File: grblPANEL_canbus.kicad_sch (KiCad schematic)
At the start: 14 parts, among them J301 Conn_01x02, U301 SN65HVD230

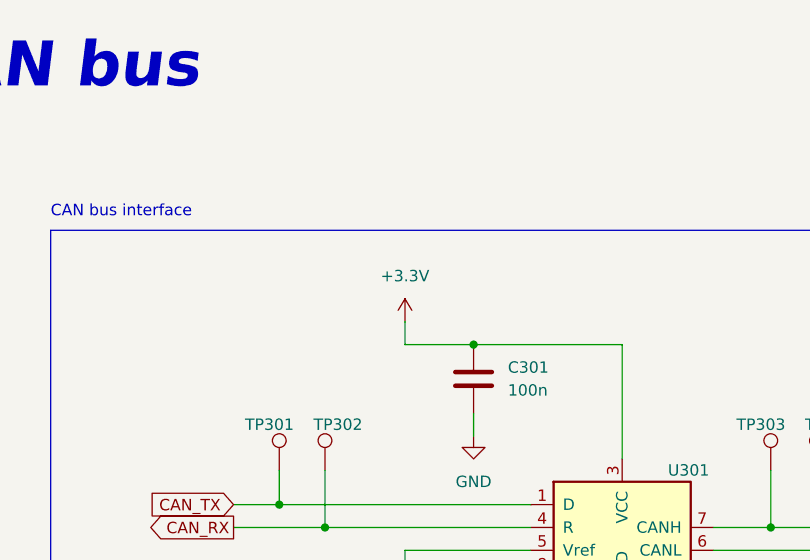
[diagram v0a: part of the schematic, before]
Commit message: ERC fixes
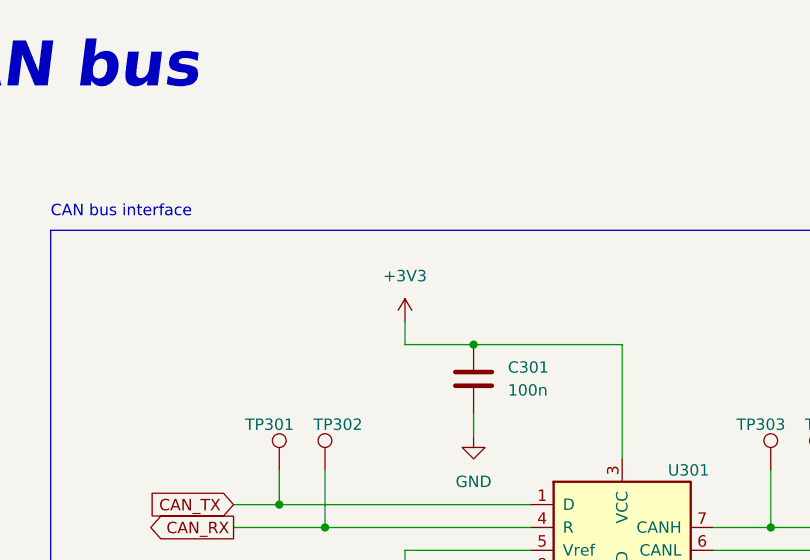
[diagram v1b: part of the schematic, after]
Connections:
- net +3.3V renamed +3V3
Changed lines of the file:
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@@
-    (pin "1")
-  )
-  (symbol (lib_id "power:+3.3V") (at 85.09 50.8 0) (unit 1)
-    (in_bom yes) (on_board yes) (fields_autoplaced)
-    (property "Reference" "#PWR0301" (id 0) (at 85.09 54.61 0)
-      (effects (font (size 1.27 1.27)) hide)
-    )
-    (property "Value" "+3.3V" (id 1) (at 85.09 45.72 0))
-    (property "Footprint" "" (id 2) (at 85.09 50.8 0)
-      (effects (font (size 1.27 1.27)) hide)
-    )
-    (property "Datasheet" "" (id 3) (at 85.09 50.8 0)
-      (effects (font (size 1.27 1.27)) hide)
-    )
     (pin "1")
   )
@@
     (pin "2")
   )
+  (symbol (lib_id "power:+3V3") (at 85.09 50.8 0) (unit 1)
+    (in_bom yes) (on_board yes) (fields_autoplaced)
+    (property "Reference" "#PWR0107" (id 0) (at 85.09 54.61 0)
+      (effects (font (size 1.27 1.27)) hide)
+    )
+    (property "Value" "+3V3" (id 1) (at 85.09 45.72 0))
+    (property "Footprint" "" (id 2) (at 85.09 50.8 0)
+      (effects (font (size 1.27 1.27)) hide)
+    )
+    (property "Datasheet" "" (id 3) (at 85.09 50.8 0)
+      (effects (font (size 1.27 1.27)) hide)
+    )
+    (pin "1")
+  )
 )

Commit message: Refresh
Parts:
- C301, C302, C303: footprint (none) -> Capacitor_SMD:C_0603_1608Metric
- D301: footprint (none) -> Package_TO_SOT_SMD:SOT-23
- J301: footprint (none) -> TerminalBlock_4Ucon:TerminalBlock_4Ucon_1x02_P3.50mm_Horizontal
- JP301: footprint (none) -> Connector_Pin:Pin_D1.1mm_L8.5mm_W2.5mm_FlatFork
- R301, R302, R303: footprint (none) -> Resistor_SMD:R_0603_1608Metric
- TP301, TP302, TP303, TP304: footprint (none) -> Connector_Pin:Pin_D1.0mm_L10.0mm
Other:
- note added: "Note: Using TI TCAN33x or SN65HVD23x transceivers, note differences in pins 5 & 8 functionality; Pin 8: SN65HVD230 and SN65HVD231 - mode select pin - strong pull down to GND = high speed mode - strong pull up to VCC = low power mode - 10kΩ to 100kΩ pull down to GND = slope control mode TCAN330 - silent mode pin - drive high for silent mode, integrated pull down SN65HVD232 and TCAN332 - not intern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"
- note added: "Refer to notes below for resistor values"
- note added: "SM712 TVS should be suitable for CAN bus (also used on modbus circuitry) - Vrwm -7v, +12v - Vbr -7.5v, +13.3v - Vc -10v, +19v (@ 1A) SN65HVD23x - maximum bus voltage at CANH or CANL = -4v to 16v - max transient voltage at CANH or CANL = -25v to 25v TCAN33x - maximum bus voltage at CANH or CANL = -14v to 14v https://www.ti.com/lit/an/slla419/slla419.pdf"
- note removed: "Notes: Using TI TCAN33x or SN65HVD23x transceivers Design for multiple parts, with differences in pins 5 & 8 functionality Pin 8: SN65HVD230 and SN65HVD231 - mode select pin - strong pull down to GND = high speed mode - strong pull up to VCC = low power mode - 10kΩ to 100kΩ pull down to GND = slope control mode TCAN330 - silent mode pin - drive high for silent mode, integrated pull down SN65HVD23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"
- note removed: "See notes for resistor values/purpose"
- moved on the sheet: C301, C302, C303, D301, J301, JP301, R301, R302, R303, TP301, TP302, TP303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

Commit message: PCB layout - WIP
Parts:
- J301: footprint TerminalBlock_4Ucon:TerminalBlock_4Ucon_1x02_P3.50mm_Horizontal -> TerminalBlock_Phoenix:TerminalBlock_Phoenix_PT-1,5-2-3.5-H_1x02_P3.50mm_Horizontal
- JP301: footprint Connector_Pin:Pin_D1.1mm_L8.5mm_W2.5mm_FlatFork -> Connector_PinHeader_2.54mm:PinHeader_1x02_P2.54mm_Vertical
- TP301, TP302, TP303, TP304: footprint Connector_Pin:Pin_D1.0mm_L10.0mm -> TestPoint:TestPoint_THTPad_D2.0mm_Drill1.0mm
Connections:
- net CONN_CANH: now reaches C302.1, D301.1 (A1), J301.1 (Pin_1), R303.1, TP303.1, U301.7 (CANH)
- net CONN_CANL: now reaches C303.2, D301.2 (A2), J301.2 (Pin_2), JP301.2 (B), TP304.1, U301.6 (CANL)
- net CAN_RS: now reaches R302.1, U301.8 (Rs)
- net CAN_VREF: now reaches R301.1, U301.5 (Vref)
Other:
- moved on the sheet: R301, R302
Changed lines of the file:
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@@
     (company "dresco")
   )
-  (junction (at 83.82 86.36) (diameter 0) (color 0 0 0 0)
+  (junction (at 82.55 86.36) (diameter 0) (color 0 0 0 0)
   )
   (junction (at 207.01 86.36) (diameter 0) (color 0 0 0 0)
@@
     (stroke (width 0) (type default) (color 0 0 0 0))
   )
-  (wire (pts (xy 83.82 73.66) (xy 83.82 76.2))
+  (wire (pts (xy 82.55 73.66) (xy 82.55 76.2))
     (stroke (width 0) (type default) (color 0 0 0 0))
   )
@@
     (stroke (width 0) (type default) (color 0 0 0 0))
   )
-  (wire (pts (xy 90.17 73.66) (xy 83.82 73.66))
+  (wire (pts (xy 82.55 73.66) (xy 90.17 73.66))
     (stroke (width 0) (type default) (color 0 0 0 0))
   )
@@
     (stroke (width 0) (type default) (color 0 0 0 0))
   )
-  (wire (pts (xy 83.82 86.36) (xy 100.33 86.36))
+  (wire (pts (xy 82.55 86.36) (xy 100.33 86.36))
     (stroke (width 0) (type default) (color 0 0 0 0))
   )
@@
     (stroke (width 0) (type default) (color 0 0 0 0))
   )
-  (wire (pts (xy 76.2 86.36) (xy 83.82 86.36))
+  (wire (pts (xy 74.93 86.36) (xy 82.55 86.36))
     (stroke (width 0) (type default) (color 0 0 0 0))
   )
@@
     (stroke (width 0) (type default) (color 0 0 0 0))
   )
-  (wire (pts (xy 76.2 71.12) (xy 90.17 71.12))
+  (wire (pts (xy 74.93 71.12) (xy 90.17 71.12))
     (stroke (width 0) (type default) (color 0 0 0 0))
   )
@@
     (stroke (width 0) (type default) (color 0 0 0 0))
   )
-  (wire (pts (xy 83.82 83.82) (xy 83.82 86.36))
+  (wire (pts (xy 82.55 83.82) (xy 82.55 86.36))
     (stroke (width 0) (type default) (color 0 0 0 0))
   )
@@
     (stroke (width 0) (type default) (color 0 0 0 0))
   )
-  (wire (pts (xy 76.2 83.82) (xy 76.2 86.36))
+  (wire (pts (xy 74.93 83.82) (xy 74.93 86.36))
     (stroke (width 0) (type default) (color 0 0 0 0))
   )
@@
     (stroke (width 0) (type default) (color 0 0 0 0))
   )
-  (wire (pts (xy 76.2 76.2) (xy 76.2 71.12))
+  (wire (pts (xy 74.93 76.2) (xy 74.93 71.12))
     (stroke (width 0) (type default) (color 0 0 0 0))
   )
@@
     (effects (font (size 1.27 1.27)) (justify left bottom))
   )
-  (text "Refer to notes below\nfor resistor values" (at 53.34 82.55 0)
+  (text "Refer to notes below\nfor resistor values" (at 52.07 82.55 0)
     (effects (font (size 1.27 1.27)) (justify left bottom))
   )
@@
   (text "Optional input protection" (at 186.69 63.5 0)
     (effects (font (size 1.27 1.27)) (justify left bottom))
+  )
+  (label "CAN_RS" (at 90.17 73.66 180)
+    (effects (font (size 1.27 1.27)) (justify right bottom))
+  )
+  (label "CONN_CANH" (at 224.79 68.58 180)
+    (effects (font (size 1.27 1.27)) (justify right bottom))
+  )
+  (label "CAN_VREF" (at 90.17 71.12 180)
+    (effects (font (size 1.27 1.27)) (justify right bottom))
+  )
+  (label "CONN_CANL" (at 224.79 86.36 180)
+    (effects (font (size 1.27 1.27)) (justify right bottom))
   )
   (global_label "CAN_RX" (shape output) (at 57.15 68.58 180) (fields_autoplaced)
@@
       (effects (font (size 1.27 1.27)) hide)
     )
-    (property "Footprint" "Connector_Pin:Pin_D1.1mm_L8.5mm_W2.5mm_FlatFork" (id 2) (at 154.94 77.47 0)
+    (property "Footprint" "Connector_PinHeader_2.54mm:PinHeader_1x02_P2.54mm_Vertical" (id 2) (at 154.94 77.47 0)
       (effects (font (size 1.27 1.27)) hide)
     )
@@
     (pin "2")
   )
-  (symbol (lib_id "Device:R") (at 83.82 80.01 0) (unit 1)
+  (symbol (lib_id "Device:R") (at 82.55 80.01 0) (unit 1)
     (in_bom yes) (on_board yes) (fields_autoplaced)
-    (property "Reference" "R302" (id 0) (at 86.36 78.7399 0)
-      (effects (font (size 1.27 1.27)) (justify left))
-    )
-    (property "Value" "10k" (id 1) (at 86.36 81.2799 0)
-      (effects (font (size 1.27 1.27)) (justify left))
-    )
-    (property "Footprint" "Resistor_SMD:R_0603_1608Metric" (id 2) (at 82.042 80.01 90)
-      (effects (font (size 1.27 1.27)) hide)
-    )
-    (property "Datasheet" "~" (id 3) (at 83.82 80.01 0)
+    (property "Reference" "R302" (id 0) (at 85.09 78.7399 0)
+      (effects (font (size 1.27 1.27)) (justify left))
+    )
+    (property "Value" "10k" (id 1) (at 85.09 81.2799 0)
+      (effects (font (size 1.27 1.27)) (justify left))
+    )
+    (property "Footprint" "Resistor_SMD:R_0603_1608Metric" (id 2) (at 80.772 80.01 90)
+      (effects (font (size 1.27 1.27)) hide)
+    )
+    (property "Datasheet" "~" (id 3) (at 82.55 80.01 0)
       (effects (font (size 1.27 1.27)) hide)
     )
@@
       (effects (font (size 1.27 1.27)) (justify left) hide)
     )
-    (property "Footprint" "Connector_Pin:Pin_D1.0mm_L10.0mm" (id 2) (at 121.92 62.23 0)
+    (property "Footprint" "TestPoint:TestPoint_THTPad_D2.0mm_Drill1.0mm" (id 2) (at 121.92 62.23 0)
       (effects (font (size 1.27 1.27)) hide)
     )
@@
       (effects (font (size 1.27 1.27)) (justify left) hide)
     )
-    (property "Footprint" "Connector_Pin:Pin_D1.0mm_L10.0mm" (id 2) (at 67.31 62.23 0)
+    (property "Footprint" "TestPoint:TestPoint_THTPad_D2.0mm_Drill1.0mm" (id 2) (at 67.31 62.23 0)
       (effects (font (size 1.27 1.27)) hide)
     )
@@
       (effects (font (size 1.27 1.27)) (justify left))
     )
-    (property "Footprint" "TerminalBlock_4Ucon:TerminalBlock_4Ucon_1x02_P3.50mm_Horizontal" (id 2) (at 229.87 76.2 0)
+    (property "Footprint" "TerminalBlock_Phoenix:TerminalBlock_Phoenix_PT-1,5-2-3.5-H_1x02_P3.50mm_Horizontal" (id 2) (at 229.87 76.2 0)
       (effects (font (size 1.27 1.27)) hide)
     )
@@
       (effects (font (size 1.27 1.27)) (justify left) hide)
     )
-    (property "Footprint" "Connector_Pin:Pin_D1.0mm_L10.0mm" (id 2) (at 72.39 62.23 0)
+    (property "Footprint" "TestPoint:TestPoint_THTPad_D2.0mm_Drill1.0mm" (id 2) (at 72.39 62.23 0)
       (effects (font (size 1.27 1.27)) hide)
     )
@@
       (effects (font (size 1.27 1.27)) (justify left) hide)
     )
-    (property "Footprint" "Connector_Pin:Pin_D1.0mm_L10.0mm" (id 2) (at 127 62.23 0)
+    (property "Footprint" "TestPoint:TestPoint_THTPad_D2.0mm_Drill1.0mm" (id 2) (at 127 62.23 0)
       (effects (font (size 1.27 1.27)) hide)
     )
@@
     (pin "8")
   )
-  (symbol (lib_id "Device:R") (at 76.2 80.01 0) (unit 1)
-    (in_bom yes) (on_board yes)
-    (property "Reference" "R301" (id 0) (at 77.47 78.74 0)
-      (effects (font (size 1.27 1.27)) (justify left))
-    )
-    (property "Value" "DNP" (id 1) (at 77.47 81.28 0)
-      (effects (font (size 1.27 1.27)) (justify left))
-    )
-    (property "Footprint" "Resistor_SMD:R_0603_1608Metric" (id 2) (at 74.422 80.01 90)
-      (effects (font (size 1.27 1.27)) hide)
-    )
-    (property "Datasheet" "~" (id 3) (at 76.2 80.01 0)
-      (effects (font (size 1.27 1.27)) hide)
-    )
+  (symbol (lib_id "Device:R") (at 74.93 80.01 0) (unit 1)
+    (in_bom yes) (on_board yes)
+    (property "Reference" "R301" (id 0) (at 76.2 78.74 0)
+      (effects (font (size 1.27 1.27)) (justify left))
+    )
+    (property "Value" "DNP" (id 1) (at 76.2 81.28 0)
+      (effects (font (size 1.27 1.27)) (justify left))
+    )
+    (property "Footprint" "Resistor_SMD:R_0603_1608Metric" (id 2) (at 73.152 80.01 90)
+      (effects (font (size 1.27 1.27)) hide)
+    )
+    (property "Datasheet" "~" (id 3) (at 74.93 80.01 0)
+      (effects (font (size 1.27 1.27)) hide)
+    )

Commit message: small cleanups
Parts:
- C302, C303: value 10p -> DNP
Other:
- note added: "Optional 10pf filter caps"
- note removed: "Optional input protection"
- moved on the sheet: D301, J301
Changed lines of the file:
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@@
   (junction (at 82.55 86.36) (diameter 0) (color 0 0 0 0)
   )
-  (junction (at 207.01 86.36) (diameter 0) (color 0 0 0 0)
+  (junction (at 209.55 86.36) (diameter 0) (color 0 0 0 0)
   )
   (junction (at 191.77 86.36) (diameter 0) (color 0 0 0 0)
@@
   (junction (at 121.92 71.12) (diameter 0) (color 0 0 0 0)
   )
-  (junction (at 207.01 68.58) (diameter 0) (color 0 0 0 0)
-  )
-  (junction (at 199.39 77.47) (diameter 0) (color 0 0 0 0)
+  (junction (at 209.55 68.58) (diameter 0) (color 0 0 0 0)
+  )
+  (junction (at 201.93 77.47) (diameter 0) (color 0 0 0 0)
   )
   (junction (at 138.43 68.58) (diameter 0) (color 0 0 0 0)
@@
     (stroke (width 0) (type default) (color 0 0 0 0))
   )
-  (polyline (pts (xy 212.09 91.44) (xy 186.69 91.44))
+  (polyline (pts (xy 199.39 91.44) (xy 185.42 91.44))
     (stroke (width 0) (type default) (color 0 0 0 0))
   )
@@
     (stroke (width 0) (type default) (color 0 0 0 0))
   )
-  (polyline (pts (xy 212.09 63.5) (xy 212.09 91.44))
-    (stroke (width 0) (type default) (color 0 0 0 0))
-  )
-  (wire (pts (xy 203.2 77.47) (xy 199.39 77.47))
+  (polyline (pts (xy 199.39 63.5) (xy 199.39 91.44))
+    (stroke (width 0) (type default) (color 0 0 0 0))
+  )
+  (wire (pts (xy 205.74 77.47) (xy 201.93 77.47))
     (stroke (width 0) (type default) (color 0 0 0 0))
   )
@@
     (stroke (width 0) (type default) (color 0 0 0 0))
   )
-  (wire (pts (xy 191.77 68.58) (xy 207.01 68.58))
-    (stroke (width 0) (type default) (color 0 0 0 0))
-  )
-  (polyline (pts (xy 186.69 63.5) (xy 212.09 63.5))
+  (wire (pts (xy 191.77 68.58) (xy 209.55 68.58))
+    (stroke (width 0) (type default) (color 0 0 0 0))
+  )
+  (polyline (pts (xy 185.42 63.5) (xy 199.39 63.5))
     (stroke (width 0) (type default) (color 0 0 0 0))
   )
@@
     (stroke (width 0) (type default) (color 0 0 0 0))
   )
-  (wire (pts (xy 224.79 78.74) (xy 224.79 86.36))
+  (wire (pts (xy 227.33 78.74) (xy 227.33 86.36))
     (stroke (width 0) (type default) (color 0 0 0 0))
   )
@@
     (stroke (width 0) (type default) (color 0 0 0 0))
   )
-  (polyline (pts (xy 186.69 63.5) (xy 186.69 91.44))
+  (polyline (pts (xy 185.42 63.5) (xy 185.42 91.44))
     (stroke (width 0) (type default) (color 0 0 0 0))
   )
@@
     (stroke (width 0) (type default) (color 0 0 0 0))
   )
-  (wire (pts (xy 199.39 77.47) (xy 191.77 77.47))
+  (wire (pts (xy 201.93 77.47) (xy 191.77 77.47))
     (stroke (width 0) (type default) (color 0 0 0 0))
   )
@@
     (stroke (width 0) (type default) (color 0 0 0 0))
   )
-  (wire (pts (xy 207.01 86.36) (xy 191.77 86.36))
+  (wire (pts (xy 209.55 86.36) (xy 191.77 86.36))
     (stroke (width 0) (type default) (color 0 0 0 0))
   )
@@
     (stroke (width 0) (type default) (color 0 0 0 0))
   )
-  (wire (pts (xy 224.79 76.2) (xy 224.79 68.58))
+  (wire (pts (xy 227.33 76.2) (xy 227.33 68.58))
     (stroke (width 0) (type default) (color 0 0 0 0))
   )
@@
     (stroke (width 0) (type default) (color 0 0 0 0))
   )
-  (wire (pts (xy 207.01 68.58) (xy 224.79 68.58))
+  (wire (pts (xy 209.55 68.58) (xy 227.33 68.58))
     (stroke (width 0) (type default) (color 0 0 0 0))
   )
@@
     (stroke (width 0) (type default) (color 0 0 0 0))
   )
-  (wire (pts (xy 199.39 77.47) (xy 199.39 80.01))
+  (wire (pts (xy 201.93 77.47) (xy 201.93 80.01))
     (stroke (width 0) (type default) (color 0 0 0 0))
   )
@@
     (stroke (width 0) (type default) (color 0 0 0 0))
   )
-  (wire (pts (xy 224.79 86.36) (xy 207.01 86.36))
+  (wire (pts (xy 227.33 86.36) (xy 209.55 86.36))
     (stroke (width 0) (type default) (color 0 0 0 0))
   )
@@
     (effects (font (size 1.27 1.27)) (justify left bottom))
   )
-  (text "Optional input protection" (at 186.69 63.5 0)
+  (text "Optional 10pf\nfilter caps" (at 185.42 63.5 0)
     (effects (font (size 1.27 1.27)) (justify left bottom))
   )
@@
     (effects (font (size 1.27 1.27)) (justify right bottom))
   )
-  (label "CONN_CANH" (at 224.79 68.58 180)
+  (label "CONN_CANH" (at 227.33 68.58 180)
     (effects (font (size 1.27 1.27)) (justify right bottom))
   )
@@
     (effects (font (size 1.27 1.27)) (justify right bottom))
   )
-  (label "CONN_CANL" (at 224.79 86.36 180)
+  (label "CONN_CANL" (at 227.33 86.36 180)
     (effects (font (size 1.27 1.27)) (justify right bottom))
   )
@@
     (pin "1")
   )
-  (symbol (lib_id "Device:D_TVS_Dual_AAC") (at 207.01 77.47 270) (unit 1)
-    (in_bom yes) (on_board yes)
-    (property "Reference" "D301" (id 0) (at 200.66 74.93 90)
-      (effects (font (size 1.27 1.27)) (justify left))
-    )
-    (property "Value" "CDSOT23-SM712" (id 1) (at 209.55 69.215 0)
-      (effects (font (size 1.27 1.27)) (justify left))
-    )
-    (property "Footprint" "Package_TO_SOT_SMD:SOT-23" (id 2) (at 207.01 73.66 0)
-      (effects (font (size 1.27 1.27)) hide)
-    )
-    (property "Datasheet" "~" (id 3) (at 207.01 73.66 0)
+  (symbol (lib_id "Device:D_TVS_Dual_AAC") (at 209.55 77.47 270) (unit 1)
+    (in_bom yes) (on_board yes)
+    (property "Reference" "D301" (id 0) (at 203.2 74.93 90)
+      (effects (font (size 1.27 1.27)) (justify left))
+    )
+    (property "Value" "CDSOT23-SM712" (id 1) (at 212.09 69.215 0)
+      (effects (font (size 1.27 1.27)) (justify left))
+    )
+    (property "Footprint" "Package_TO_SOT_SMD:SOT-23" (id 2) (at 209.55 73.66 0)
+      (effects (font (size 1.27 1.27)) hide)
+    )
+    (property "Datasheet" "~" (id 3) (at 209.55 73.66 0)
       (effects (font (size 1.27 1.27)) hide)
     )
@@
     (pin "2")
   )
-  (symbol (lib_id "Connector_Generic:Conn_01x02") (at 229.87 76.2 0) (unit 1)
+  (symbol (lib_id "Connector_Generic:Conn_01x02") (at 232.41 76.2 0) (unit 1)
     (in_bom yes) (on_board yes) (fields_autoplaced)
-    (property "Reference" "J301" (id 0) (at 232.41 76.1999 0)
-      (effects (font (size 1.27 1.27)) (justify left))
-    )
-    (property "Value" "Conn_01x02" (id 1) (at 232.41 78.7399 0)
-      (effects (font (size 1.27 1.27)) (justify left))
-    )
-    (property "Footprint" "TerminalBlock_Phoenix:TerminalBlock_Phoenix_PT-1,5-2-3.5-H_1x02_P3.50mm_Horizontal" (id 2) (at 229.87 76.2 0)
-      (effects (font (size 1.27 1.27)) hide)
-    )
-    (property "Datasheet" "~" (id 3) (at 229.87 76.2 0)
-      (effects (font (size 1.27 1.27)) hide)
-    )
-    (pin "1")
-    (pin "2")
-  )
-  (symbol (lib_id "power:GND") (at 199.39 80.01 0) (unit 1)
-    (in_bom yes) (on_board yes)
-    (property "Reference" "#PWR0304" (id 0) (at 199.39 86.36 0)
-      (effects (font (size 1.27 1.27)) hide)
-    )
-    (property "Value" "GND" (id 1) (at 200.66 83.82 0)
-      (effects (font (size 1.27 1.27)) hide)
-    )
-    (property "Footprint" "" (id 2) (at 199.39 80.01 0)
-      (effects (font (size 1.27 1.27)) hide)
-    )
-    (property "Datasheet" "" (id 3) (at 199.39 80.01 0)
+    (property "Reference" "J301" (id 0) (at 234.95 76.1999 0)
+      (effects (font (size 1.27 1.27)) (justify left))
+    )
+    (property "Value" "Conn_01x02" (id 1) (at 234.95 78.7399 0)
+      (effects (font (size 1.27 1.27)) (justify left))
+    )
+    (property "Footprint" "TerminalBlock_Phoenix:TerminalBlock_Phoenix_PT-1,5-2-3.5-H_1x02_P3.50mm_Horizontal" (id 2) (at 232.41 76.2 0)
+      (effects (font (size 1.27 1.27)) hide)
+    )
+    (property "Datasheet" "~" (id 3) (at 232.41 76.2 0)
+      (effects (font (size 1.27 1.27)) hide)
+    )
+    (pin "1")
+    (pin "2")
+  )
+  (symbol (lib_id "power:GND") (at 201.93 80.01 0) (unit 1)
+    (in_bom yes) (on_board yes)
+    (property "Reference" "#PWR0304" (id 0) (at 201.93 86.36 0)
+      (effects (font (size 1.27 1.27)) hide)
+    )
+    (property "Value" "GND" (id 1) (at 203.2 83.82 0)
+      (effects (font (size 1.27 1.27)) hide)
+    )
+    (property "Footprint" "" (id 2) (at 201.93 80.01 0)
+      (effects (font (size 1.27 1.27)) hide)
+    )
+    (property "Datasheet" "" (id 3) (at 201.93 80.01 0)
       (effects (font (size 1.27 1.27)) hide)
     )
@@
       (effects (font (size 1.27 1.27)) (justify left))
     )
-    (property "Value" "10p" (id 1) (at 193.04 85.09 0)
+    (property "Value" "DNP" (id 1) (at 193.04 85.09 0)
       (effects (font (size 1.27 1.27)) (justify left))
     )
@@
       (effects (font (size 1.27 1.27)) (justify left))
     )
-    (property "Value" "10p" (id 1) (at 193.04 74.93 0)
-      (effects (font (size 1.27 1.27)) (justify left))
-    )
+    (property "Value" "DNP" (id 1) (at 193.04 74.93 0)
+      (effects (font (size 1.27 1.27)) (justify left))
+    )
